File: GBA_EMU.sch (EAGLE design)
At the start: 103 parts, among them J1 USB-MINIB-5PIN, J2 AVR_SPI, SW1 LEFT, SW2 RIGHT, SW3 PWR_SWITCH, SW8 OS102011MA1Q, U1 MIC7221, U2 MCP1642B-ADJ, U4 LM4875, U5 Mic5365-2.8Y, U7 AZV321, X2 HEADPHONE

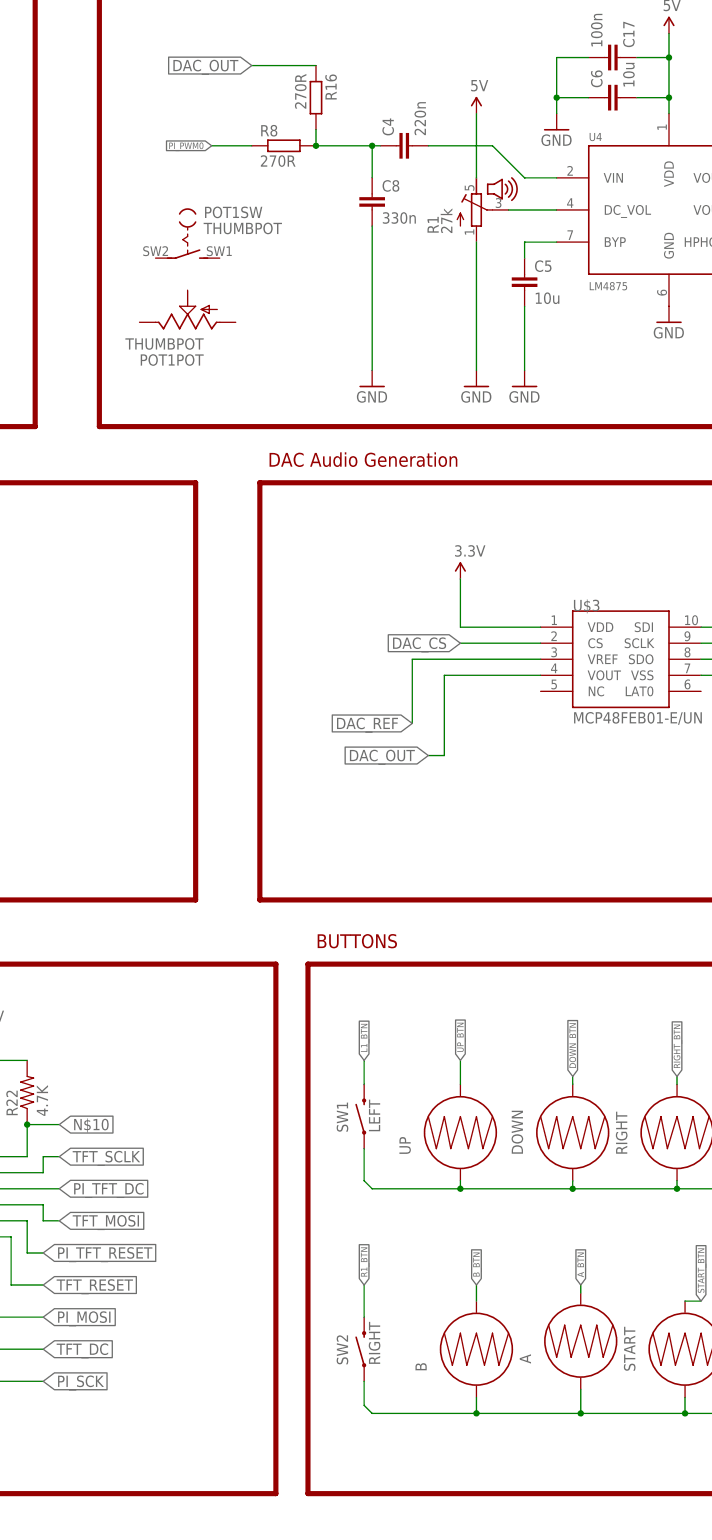
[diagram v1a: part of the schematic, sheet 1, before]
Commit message: adding more power chips
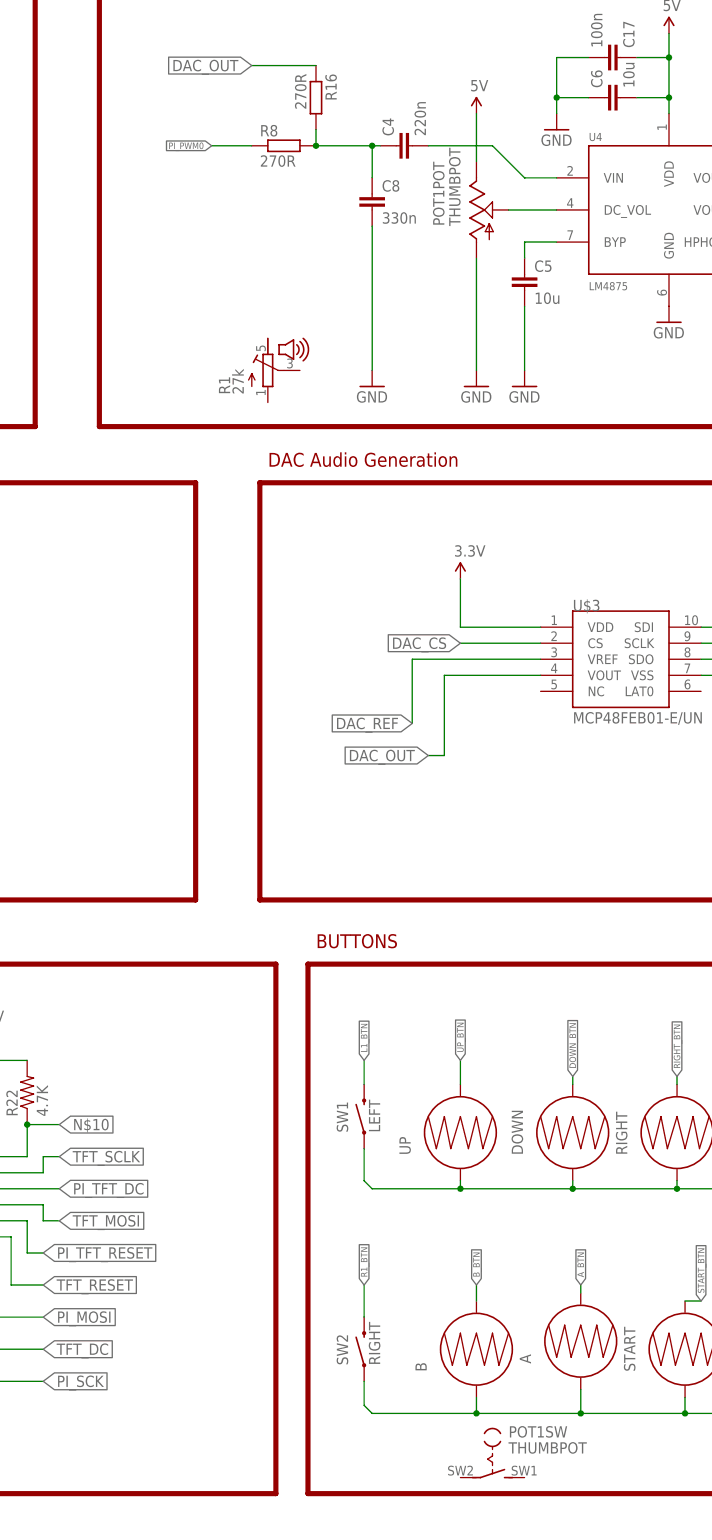
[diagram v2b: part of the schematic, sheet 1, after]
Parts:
- added J3, J4: FTDI_DEVICE, SparkFun-Connectors:FTDI_DEVICE
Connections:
- net 5V: now also POT1POT.E; no longer R1.E
- net GND: now also J3.GND, J4.GND, POT1POT.A; no longer R1.A
- net N$8: now also POT1POT.S; no longer R1.S
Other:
- note added: "FTDI Connectors"
- note removed: "MicroSD Card"
- moved on the sheet: POT1POT, POT1SW, R1
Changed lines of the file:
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@@
 <part name="D8" library="adafruit" deviceset="DIODE" device="SOD-523"/>
 <part name="SUPPLY19" library="SparkFun-Aesthetics" deviceset="3.3V" device=""/>
+<part name="J3" library="SparkFun-Connectors" deviceset="FTDI_DEVICE" device=""/>
+<part name="J4" library="SparkFun-Connectors" deviceset="FTDI_DEVICE" device=""/>
+<part name="GND40" library="SparkFun-Aesthetics" deviceset="GND" device=""/>
+<part name="GND41" library="SparkFun-Aesthetics" deviceset="GND" device=""/>
 </parts>
 <sheets>
@@
 <instance part="UP" gate="S$1" x="332.74" y="24.13" rot="R90"/>
 <instance part="START" gate="G$1" x="368.3" y="-10.16" rot="R90"/>
-<instance part="R1" gate="R$1" x="335.28" y="170.18"/>
+<instance part="R1" gate="R$1" x="302.26" y="144.78"/>
 <instance part="DOWN" gate="S$1" x="350.52" y="24.13" rot="R90"/>
 <instance part="LEFT" gate="S$1" x="383.54" y="24.13" rot="R90"/>
@@
 <instance part="R22" gate="G$1" x="264.16" y="30.48" rot="R90"/>
 <instance part="SUPPLY27" gate="G$1" x="256.54" y="38.1"/>
-<instance part="POT1" gate="SW" x="289.56" y="162.56"/>
-<instance part="POT1" gate="POT" x="289.56" y="152.4"/>
+<instance part="POT1" gate="SW" x="337.82" y="-30.48"/>
+<instance part="POT1" gate="POT" x="335.28" y="170.18" rot="R270"/>
 </instances>
 <busses>
@@
 <pinref part="GND11" gate="1" pin="GND"/>
 <wire x1="318.77" y1="167.64" x2="318.77" y2="144.78" width="0.1524" layer="91"/>
-</segment>
-<segment>
-<pinref part="R1" gate="R$1" pin="A"/>
-<pinref part="GND7" gate="1" pin="GND"/>
-<wire x1="335.28" y1="165.1" x2="335.28" y2="144.78" width="0.1524" layer="91"/>
 </segment>
 <segment>
@@
 <wire x1="464.82" y1="160.02" x2="464.82" y2="157.48" width="0.1524" layer="91"/>
 </segment>
+<segment>
+<pinref part="POT1" gate="POT" pin="A"/>
+<pinref part="GND7" gate="1" pin="GND"/>
+<wire x1="335.28" y1="162.56" x2="335.28" y2="144.78" width="0.1524" layer="91"/>
+</segment>
 </net>
 <net name="!PWREN" class="0">
@@
 </net>
 <net name="5V" class="0">
-<segment>
-<pinref part="SUPPLY2" gate="G$1" pin="5V"/>
-<pinref part="R1" gate="R$1" pin="E"/>
-<wire x1="335.28" y1="185.42" x2="335.28" y2="175.26" width="0.1524" layer="91"/>
-</segment>
 <segment>
 <pinref part="SUPPLY3" gate="G$1" pin="5V"/>
@@
 <wire x1="441.96" y1="177.8" x2="441.96" y2="195.58" width="0.1524" layer="91"/>
 </segment>
+<segment>
+<pinref part="POT1" gate="POT" pin="E"/>
+<pinref part="SUPPLY2" gate="G$1" pin="5V"/>
+<wire x1="335.28" y1="177.8" x2="335.28" y2="185.42" width="0.1524" layer="91"/>
+</segment>
 </net>
 <net name="PI_PWM0" class="0">
@@
 <wire x1="309.88" y1="182.88" x2="309.88" y2="180.34" width="0.1524" layer="91"/>
 <junction x="309.88" y="180.34"/>
-</segment>
-</net>
-<net name="N$8" class="0">
-<segment>
-<pinref part="U4" gate="U$1" pin="DC_VOL"/>
-<pinref part="R1" gate="R$1" pin="S"/>
-<wire x1="347.98" y1="170.18" x2="340.36" y2="170.18" width="0.1524" layer="91"/>
 </segment>
 </net>
@@
 <wire x1="254" y1="15.24" x2="269.24" y2="15.24" width="0.1524" layer="91"/>
 <label x="269.24" y="15.24" size="1.778" layer="95" xref="yes"/>
+</segment>
+</net>
+<net name="N$8" class="0">
+<segment>
+<pinref part="U4" gate="U$1" pin="DC_VOL"/>
+<pinref part="POT1" gate="POT" pin="S"/>
+<wire x1="347.98" y1="170.18" x2="340.36" y2="170.18" width="0.1524" layer="91"/>
 </segment>
 </net>
@@
 <wire x1="7.62" y1="7.62" x2="7.62" y2="40.64" width="0.4064" layer="94"/>
 <text x="167.64" y="170.18" size="1.778" layer="94">USB Hub</text>
-<text x="167.894" y="115.57" size="1.778" layer="94">MicroSD Card</text>
+<text x="167.894" y="115.57" size="1.778" layer="94">FTDI Connectors</text>
 <text x="8.128" y="41.656" size="1.778" layer="94">Test Points</text>
 </plain>
@@
 <instance part="D8" gate="G$1" x="127" y="91.44" rot="R180"/>
 <instance part="SUPPLY19" gate="G$1" x="30.48" y="142.24"/>
+<instance part="J3" gate="G$1" x="231.14" y="96.52"/>
+<instance part="J4" gate="G$1" x="231.14" y="66.04"/>
+<instance part="GND40" gate="1" x="223.52" y="78.74"/>
+<instance part="GND41" gate="1" x="223.52" y="48.26"/>
 </instances>
 <busses>
@@
 <pinref part="GND38" gate="1" pin="GND"/>
 </segment>
-</net>
+<segment>
+<pinref part="J3" gate="G$1" pin="GND"/>
+<wire x1="226.06" y1="88.9" x2="223.52" y2="88.9" width="0.1524" layer="91"/>
+<wire x1="223.52" y1="88.9" x2="223.52" y2="81.28" width="0.1524" layer="91"/>
+<pinref part="GND40" gate="1" pin="GND"/>
+</segment>
+<segment>
+<pinref part="J4" gate="G$1" pin="GND"/>
+<wire x1="226.06" y1="58.42" x2="223.52" y2="58.42" width="0.1524" layer="91"/>
+<wire x1="223.52" y1="58.42" x2="223.52" y2="50.8" width="0.1524" layer="91"/>
+<pinref part="GND41" gate="1" pin="GND"/>
+</segment>
+</net>

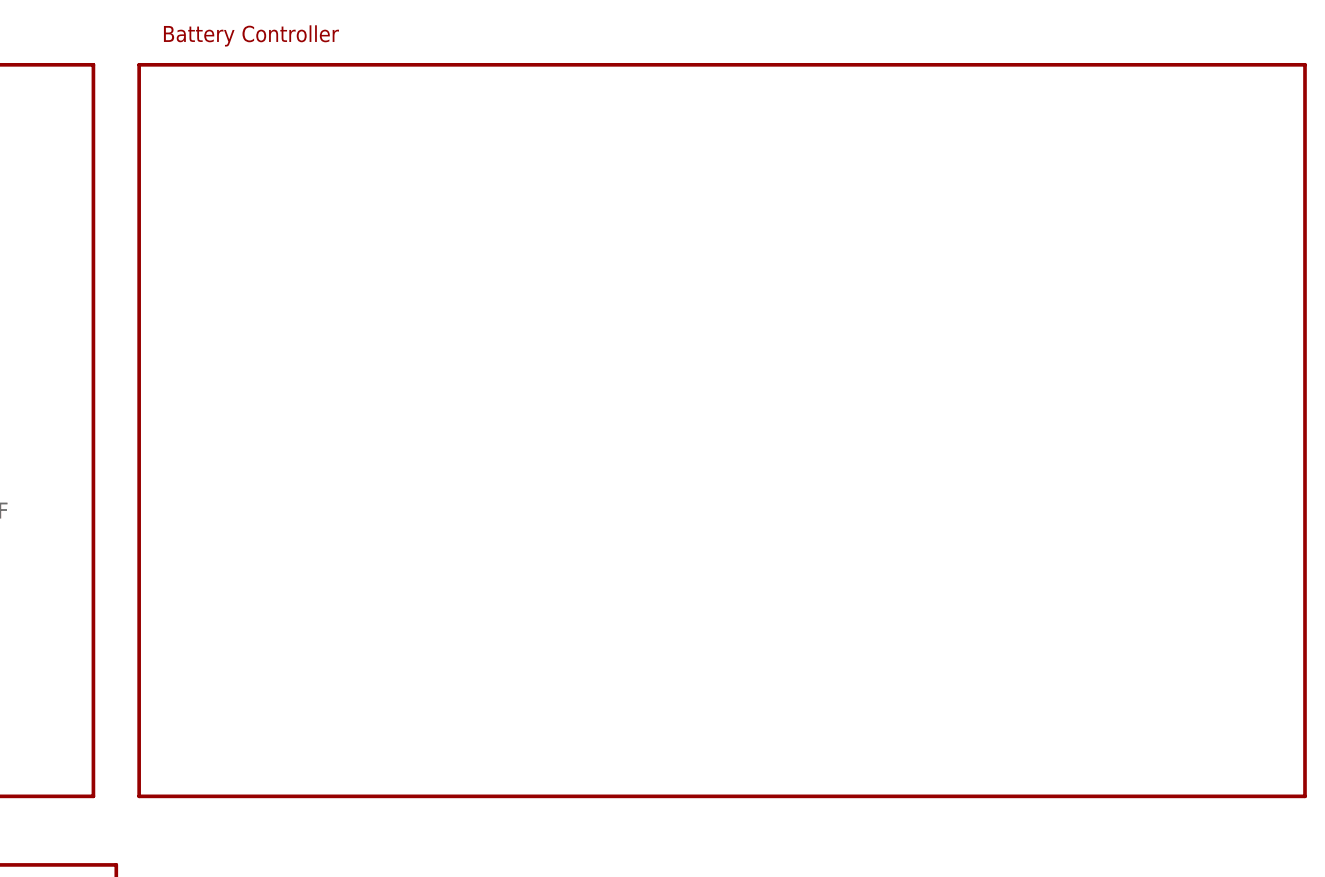
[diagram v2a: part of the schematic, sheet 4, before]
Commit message: added a few grounding caps
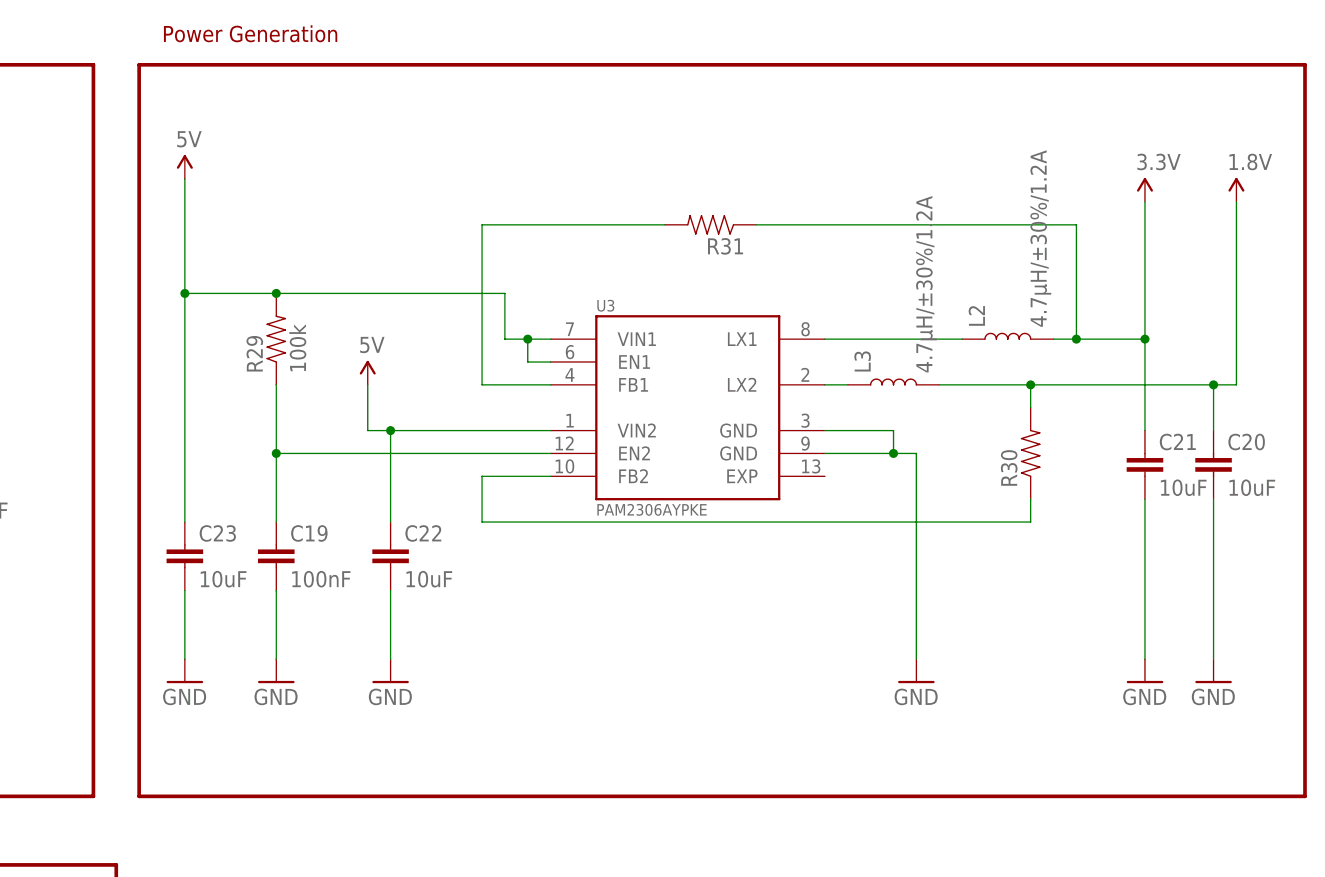
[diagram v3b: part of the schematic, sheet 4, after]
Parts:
- added C19: 100nF, SparkFun-Capacitors:10NF/10000PF-50V-10%(0603)
- added C20, C21, C22, C23: 10uF, SparkFun-Capacitors:10UF-6.3V-20%(0603)
- added L2, L3: 4.7µH/±30%/1.2A, SparkFun-Coils:INDUCTOR-CDRH-4.7UH
- added R29: 100k, SparkFun-Resistors:100KOHM-1/10W-1%(0603)
- added R30, R31: (no value), SparkFun-Resistors:RESISTOR0805-RES
- added U3: PAM2306AYPKE, custom:PAM2306AYPKE
- J3, J4: value FTDI_DEVICE -> FTDI_DEVICERA_SMT; device SparkFun-Connectors:FTDI_DEVICE -> SparkFun-Connectors:FTDI_DEVICERA_SMT
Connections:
- new net N$32: L3.1, U3.LX2
- new net N$46: C19.1, R29.1, U3.EN2
- new net N$47: L2.1, U3.LX1
- new net N$49: R31.2, U3.FB1
- new net N$50: R30.1, U3.FB2
- net 1.8V: now also C20.1, L3.2, R30.2
- net 3.3V: now also C21.1, L2.2, R31.1
- net 5V: now also C22.1, C23.1, R29.2, U3.EN1, U3.VIN1, U3.VIN2
- net GND: now also C19.2, C20.2, C21.2, C22.2, C23.2, U3.GND@1, U3.GND@2
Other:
- note added: "Power Generation"
- note removed: "Battery Controller"

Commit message: changed advanced schematic to Pi64 and added Ryan's version
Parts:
- removed C19: 100nF, SparkFun-Capacitors:10NF/10000PF-50V-10%(0603)
- removed C20, C21, C22, C23: 10uF, SparkFun-Capacitors:10UF-6.3V-20%(0603)
- removed COPRO: MEGA16u2, adafruit:ATMEGA32U2-TQFP
- removed D4, D7, D8: (no value), adafruit:DIODESOD-523
- removed D5, D6: DIODE_DFLS130L, custom:DIODE_DFLS130L
- removed FAN: (no value), SparkFun-Connectors:M02PTH
- removed FRAME2: FRAME-LEDGER, SparkFun-Aesthetics:FRAME-LEDGER
- removed J1: USB-MINIB-5PIN, SparkFun-Connectors:USB-MINIB-5PIN
- removed J2: AVR_SPI, SparkFun-Connectors:AVR_SPI_PRG_6PTH
- removed J3, J4: FTDI_DEVICERA_SMT, SparkFun-Connectors:FTDI_DEVICERA_SMT
- removed L2, L3: 4.7µH/±30%/1.2A, SparkFun-Coils:INDUCTOR-CDRH-4.7UH
- removed PCB1: RPI_COMPUTE, e14_Rpi_Compute_RevC:RPI_COMPUTE
- removed POT1: THUMBPOT, adafruit:THUMBPOT
- removed R$1: 976kR, SparkFun-Resistors:820KOHM-1/10W-1%(0603)
- removed R$8: 430kR, SparkFun-Resistors:820KOHM-1/10W-1%(0603)
- removed R16: 270R, rcl:R-EU_R0805
- removed R17, R18: 22, SparkFun-Resistors:22OHM1/10W1%(0603)
- removed R19, R24, R27, R28: 10K, SparkFun-Resistors:10KOHM-1/10W-1%(0603)0603
- removed R20: 680, SparkFun-Resistors:680OHM1/10W5%(0603)
- removed R21, R22, R25, R26: 4.7K, SparkFun-Resistors:4.7KOHM-1/10W-1%(0603)
- removed R23, R29: 100k, SparkFun-Resistors:100KOHM-1/10W-1%(0603)
- removed R30, R31: (no value), SparkFun-Resistors:RESISTOR0805-RES
- removed SW4, SW5: (no value), adafruit:SWITCH_PUSHBUTTONEVQ-PE
- removed SW6, SW7: (no value), adafruit:SWITCH_PUSHBUTTONSOFTTOUCHSMD_SJ
- removed SW8: OS102011MA1Q, adafruit:OS102011MA1Q
- removed T1: (no value), custom:TRANSISTOR_PNP_DRIVERMUN2111T1SC59-BEC
- removed TM1: (no value), adafruit:TRIMPOTTC33X
- removed TP1, TP2, TP3, TP4, TP5, TP6, TP7: PTR1TP12R, testpad:PTR1TP12R
- removed U$1: CBT3244AD, custom:CBT3244AD
- removed U$2: LOGO2INCH_SVG, custom:LOGO2INCH_SVG
- removed U$3: MCP48FEB01-E/UN, custom:MCP48FEB01-E/UN
- removed U$5: CRYSTAL-ABLS, custom:CRYSTAL-ABLS
- added L4: 4.7uH, rcl:L-EUWE-TPC
- added Q1: MOSFET-PCHANNEL, SparkFun-DiscreteSemi:MOSFET-PCHANNEL
- added U6: MIC7221, SparkFun-AnalogIC:MIC7221
- BT1: value (none) -> ~3V; device custom:GBA_BATTERY -> GBA:BATTERY
- C1: value 100nF -> 100n; device SparkFun-Capacitors:CAP0603-CAP -> rcl:C-EUC0805
- C10: value 1.0uF -> 47uF; device SparkFun-Capacitors:1.0UF-16V-10%(0603) -> rcl:CPOL-EU153CLV-0405
- C11, C12: value 22pF -> 100n; device SparkFun-Capacitors:22PF-50V-5%(0603) -> rcl:C-EUC0805
- C14: value 47uF -> 10u; device SparkFun-Capacitors:47UF-10V-10%(TANT) -> rcl:C-EUC0805
- C16: value 47uF -> 100n; device SparkFun-Capacitors:47UF-10V-10%(TANT) -> rcl:C-EUC0805
- C2: value 100nF -> 10u; device SparkFun-Capacitors:CAP0603-CAP -> rcl:C-EUC0805
- C3: value 100nF -> 100n; device SparkFun-Capacitors:10PF-50V-5%(0603) -> rcl:C-EUC0805
- C9: value 4.7u -> 47uF; device rcl:C-EUC1608 -> rcl:CPOL-EU153CLV-0405
- D1: value DUAL_LED -> DFLS130L; device custom:DUAL_LED -> diode:DFLS130L
- D2: value (none) -> DFLS130L; device adafruit:DIODESOD-523 -> diode:DFLS130L
- D3: value (none) -> DUAL_LED; device adafruit:DIODESOD-523 -> GBA:DUAL_LED
- L1: value 4.7uH -> 600; device SparkFun-Passives:INDUCTORINDUCTOR_4.7UH -> SparkFun-Passives:INDUCTOR0805
- R11: value 100K -> 47k; device rcl:R-US_R0805 -> adafruit:TRIMPOTTC33X
- R12: value 1K -> 620R; device SparkFun-Resistors:1KOHM-1/10W-1%(0603) -> rcl:R-EU_R0805
- R13: value 4.7K -> 620R; device SparkFun-Resistors:4.7KOHM-1/10W-1%(0603) -> rcl:R-EU_R0805
- R14: value 100K -> 100k; device rcl:R-US_R0805 -> rcl:R-EU_R0805
- R15: value 100K -> 270R; device rcl:R-US_R0805 -> rcl:R-EU_R0805
- R2: value 4.7K -> 27R; device SparkFun-Resistors:4.7KOHM-1/10W-1%(0603) -> rcl:R-EU_R0805
- R3: value 100k -> 27R; device SparkFun-Resistors:100KOHM-1/10W-1%(0603) -> rcl:R-EU_R0805
- R4: value 270 -> 1k; device SparkFun-Resistors:287OHM-1/10W-1%(0603) -> rcl:R-EU_R0805
- R5: value 680 -> 100k; device SparkFun-Resistors:680OHM1/10W5%(0603) -> rcl:R-EU_R0805
- R7: value 0R -> 976k; device rcl:R-EU_R2012 -> rcl:R-EU_R0805
- R9: value 100K -> 430k; device rcl:R-US_R0805 -> rcl:R-EU_R0805
- U1: value MIC7221 -> RPI-ZERO; device custom:SPARKFUN-ANALOGIC_MIC7221 -> RPI-Zero:RPI-ZERO
- U2: value MCP1642B-ADJ -> FT230X; device custom:MICROCHIP_MCP1642B-ADJ -> ftdichip:FT230X
- U3: value PAM2306AYPKE -> MCP1642B-ADJ; device custom:PAM2306AYPKE -> microchip:MCP1642B-ADJ
- U5: value Mic5365-2.8Y -> V_REG_LDOSMD2
- X1: value (none) -> LINK_SOCKET; device Adafruit_PowerBoost:MICROBUILDER_USB_TYPEAPTHFML -> GBA:LINK_SOCKET
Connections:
- removed net 1.8V: C20.1, L3.2, PCB1.183/1V8, PCB1.184/1V8, PCB1.185/1V8, PCB1.186/1V8, R30.2, TP5.TP
- removed net BATT_LOW: D1.1, D1.3, D8.A, R3.2, U1.OUT1
- removed net COPRO_D+: R18.1
- removed net COPRO_D-: R17.1
- removed net COPRO_DC: COPRO.PB6(PCINT6), U$1.1A4
- removed net COPRO_MISO: COPRO.PB3(PDO/MISO/PCINT3), J2.1, U$3.SDO
- removed net COPRO_MOSI: COPRO.PB2(PDI/MOSI/PCINT2), J2.4, U$1.1A2, U$3.SDI
- removed net COPRO_RESET: COPRO./RESET(PC1), J2.5, R19.1
- removed net COPRO_RX: COPRO.PD2(INT2/AIN1/RXD1)
- removed net COPRO_SCK: COPRO.PB1(SCK/PCINT1), J2.3, U$1.1A1, U$3.SCLK
- removed net COPRO_TFT_RESET: COPRO.PB0(SS/PCINT0), U$1.1A3
- removed net COPRO_TX: COPRO.PD3(INT3/TXD1)
- removed net DAC_CS: COPRO.PB5(PCINT5), U$3.CS
- removed net DAC_OUT: R16.1, U$3.VOUT
- removed net DAC_REF: U$3.VREF
- removed net DOWN_BTN: DOWN.2, PCB1.59/GPIO17
- removed net EMMC_DISABLE: PCB1.2/EMMC_DISABLE_N
- removed net FAN_EN: R12.2
- removed net HDMI_CEC: PCB1.171/HDMI_CEC
- removed net HDMI_CLK_N: PCB1.111/HDMI_CK_N*
- removed net HDMI_CLK_P: PCB1.113/HDMI_CK_P*
- removed net HDMI_D0_N: PCB1.117/HDMI_D0_N*
- removed net HDMI_D0_P: PCB1.119/HDMI_D0_P*
- removed net HDMI_D1_N: PCB1.123/HDMI_D1_N*
- removed net HDMI_D1_P: PCB1.125/HDMI_D1_P*
- removed net HDMI_D2_N: PCB1.129/HDMI_D2_N*
- removed net HDMI_D2_P: PCB1.131/HDMI_D2_P*
- removed net HDMI_SCLK: PCB1.175/HDMI_SCL
- removed net HDMI_SDA: PCB1.173/HDMI_SDA
- removed net L1_BTN: PCB1.21/GPIO6, SW1.2
- removed net L2_BTN: PCB1.57/GPIO16, R2.1, SW4.P$1
- removed net LEFT_BTN: LEFT.2, PCB1.89/GPIO27
- removed net N$17: PCB1.28/GPIO28, R9.2
- removed net N$26: R14.2
- removed net N$27: R15.2
- removed net N$28: C11.1, COPRO.XTAL1, U$5.P$2
- removed net N$29: C12.1, COPRO.XTAL2/PC0, U$5.P$1
- removed net N$30: PCB1.179/VDD_CORE
- removed net N$31: D3.A, D4.C
- removed net N$32: L3.1, U3.LX2
- removed net N$33: D3.C, D7.C, R27.2, R28.2
- removed net N$34: L1.2, U2.SW
- removed net N$35: PCB1.177/RUN
- removed net N$36: PCB1.197/VBAT, PCB1.199/VBAT
- removed net N$37: PCB1.198/VBAT, PCB1.200/VBAT
- removed net N$38: COPRO.PC7(ICP1/INT4/CLKO), R27.1
- removed net N$39: FAN.1, T1.C
- removed net N$40: R12.1, T1.B
- removed net N$41: PCB1.23/GPIO7
- removed net N$42: PCB1.27/GPIO8
- removed net N$43: PCB1.29/GPIO9
- removed net N$44: COPRO.PD0(INT0/OC0B), R24.1
- removed net N$45: C14.+, D5.C, D6.C, L1.1, SW8G$1.P, U2.VIN
- removed net N$46: C19.1, R29.1, U3.EN2
- removed net N$47: L2.1, U3.LX1
- removed net N$49: R31.2, U3.FB1
- removed net N$50: R30.1, U3.FB2
- removed net PI_MOSI: PCB1.33/GPIO10, U$1.2A2
- removed net PI_PWM0: PCB1.63/GPIO18, R8.1
- removed net PI_SCK: PCB1.35/GPIO11, U$1.2A1
- removed net PI_SHUTDOWN: PCB1.69/GPIO20
- removed net PI_TFT_DC: PCB1.11/GPIO3, U$1.2A4
- removed net PI_TFT_RESET: PCB1.9/GPIO2, U$1.2A3
- removed net PWR_DOWN: D2.A, D4.A, SW8G$1.S
- removed net PWR_UP: D2.C, R23.2, R24.2, U2.EN
- removed net R1_BTN: PCB1.71/GPIO21, SW2.2
- removed net R2_BTN: PCB1.45/GPIO12, R13.1, SW5.P$1
- removed net RIGHT_BTN: PCB1.75/GPIO22, RIGHT.2
- removed net SELECT_BTN: PCB1.81/GPIO24, SEL.2
- removed net START_BTN: PCB1.77/GPIO23, START.2
- removed net TFT_SCLK: TFT1.SCL, U$1.1B1, U$1.2B1
- removed net UP_BTN: PCB1.17/GPIO5, UP.2
- removed net USB_GND: J1.GND
- removed net V_BATT: BT1.+, D6.A, R4.2
- removed net V_USB: D5.A, J1.VBUS
- removed net X_BTN: PCB1.83/GPIO25, R26.1, SW6.P$1
- removed net Y_BTN: PCB1.47/GPIO13, R25.1, SW7.P$1
- new net !PWREN: C3.2, Q1.G, R4.1, R5.2
- new net 0.8128: C9.+, L4.1, SW3.P, U3.EN, U3.VIN
- new net 3.3V_FTDI: C1.1, U2.!RESET, U2.3V3OUT, U2.VCCIO
- new net 5V_FTDI: C14.1, C2.1, L1.1, Q1.S, R5.1, U2.VCC
- new net DOWN: DOWN.2, U1.GPIO17/GEN0
- new net LEFT: LEFT.2, U1.GPIO27/GEN2
- new net LEFT_BUMP: SW1.2, U1.GPIO6
- new net PWM0: R8.1, U1.GPIO18
- new net RIGHT: RIGHT.2, U1.GPIO22/GEN3
- new net RIGHT_BUMP: SW2.2, U1.GPIO21
- new net SELECT: SEL.2, U1.GEN5/GPIO24
- new net START: START.2, U1.GEN4/GPIO23
- new net TFT_SCK: TFT1.SCL, U1.GPIO11/SCLK
- new net UP: U1.GPIO5, UP.2
- new net USB_5V: C3.1, D1.A, Q1.D
- new net V_BAT: BT1.+, D2.A, R15.2
- net 2.8V: no longer TP3.TP
- net 3.3V: now also U1.3V3@1; no longer C21.1, COPRO.AVCC, COPRO.UVCC, COPRO.VCC, L2.2, PCB1.191/3V3, PCB1.192/3V3, PCB1.193/3V3, PCB1.194/3V3, PCB1.39/GPIO0-27_VREF, PCB1.40/GPIO0-27_VREF, R13.2, R2.2, R21.2, R22.2, R25.2, R26.2, R31.1, R7.2, TP2.TP, U$1.VCC, U$3.VDD
- net 5V: now also C10.+, C16.1, R1.E, R11.E, R13.2, R7.2, U1.5V0@1, U1.5V0@2, U3.VOUT, U6.+V; no longer C16.+, C22.1, C23.1, C3.1, FAN.2, J2.2, POT1POT.E, R$1.2, R19.2, R29.2, R5.2, TM1.E, TP1.TP, U1.+V, U2.VOUT, U3.EN1, U3.VIN1, U3.VIN2, X1.VBUS
- net A_BTN: now also U1.GPIO19; no longer PCB1.65/GPIO19
- net B_BTN: now also U1.GPIO26; no longer PCB1.87/GPIO26
- net GND: now also C10.-, C14.2, C16.2, C9.-, R1.A, R11.A, R12.2, U1.GND@2, U1.GND@3, U1.GND@4, U1.GND@5, U1.GND@6, U1.GND@7, U1.GND@8, U2.GND@1, U2.GND@2, U3.GND, U6.GND, X1.1; no longer C10.2, C14.-, C16.-, C19.2, C20.2, C21.2, C22.2, C23.2, C3.2, C9.2, COPRO.GND, COPRO.UGND, J2.6, J3.GND, J4.GND, PCB1.1/GND, PCB1.103/GND, PCB1.104/GND, PCB1.109/GND, PCB1.110/GND, PCB1.115/GND, PCB1.116/GND, PCB1.121/GND, PCB1.122/GND, PCB1.127/GND, PCB1.13/GND, PCB1.133/GND, PCB1.134/GND, PCB1.139/GND, PCB1.14/NC, PCB1.140/GND, PCB1.145/GND, PCB1.146/GND, PCB1.151/GND, PCB1.152/GND, PCB1.157/GND, PCB1.163/GND, PCB1.164/GND, PCB1.169/GND, PCB1.170/GND, PCB1.181/GND, PCB1.182/GND, PCB1.187/GND, PCB1.188/GND, PCB1.19/GND, PCB1.195/GND, PCB1.196/GND, PCB1.20/NC, PCB1.25/GND, PCB1.26/GND, PCB1.31/GND, PCB1.32/GND, PCB1.37/GND, PCB1.38/GND, PCB1.43/GND, PCB1.44/GND, PCB1.49/GND, PCB1.50/GND, PCB1.55/GND, PCB1.56/GND, PCB1.61/GND, PCB1.62/GND, PCB1.67/GND, PCB1.68/GND, PCB1.7/GND, PCB1.73/GND, PCB1.74/GND, PCB1.79/GND, PCB1.8/NC, PCB1.80/GND, PCB1.85/GND, PCB1.86/GND, PCB1.91/GND, PCB1.92/GND, PCB1.97/GND, PCB1.98/GND, POT1POT.A, R$8.1, R11.1, R14.1, R15.1, R20.1, R23.1, SW4.P$2, SW5.P$2, SW6.P$2, SW7.P$2, T1.E, TM1.A, TP4.TP, U$1.GND, U$3.VSS, U1.GND, U2.GND, U3.GND@1, U3.GND@2
- net N$1: now also C11.1, R11.S, R14.2, U6.+IN1; no longer C9.1, PCB1.4/NC, PCB1.6/NC, R7.1
- net N$10: now also R4.2, U2.CBUS3; no longer R22.1, U$1.2!OE
- net N$12: now also L4.2, U3.SW; no longer COPRO.PC2(AIN2/PCIN11), R28.1
- net N$18: now also D1.C, D2.C, SW3.O; no longer R21.1, U$1.!1OE
- net N$19: now also D3.1, D3.3, R14.1, U6.OUT1; no longer COPRO.D-, R17.2
- net N$2: no longer R16.2
- net N$20: now also R7.1, R9.2, U3.VFB; no longer PCB1.30/GPIO29, R11.2
- net N$22: now also D3.4, R13.1; no longer COPRO.D+, R18.2
- net N$23: now also D3.2, R12.1; no longer R$1.1, R$8.2, U2.VFB
- net N$25: now also C12.1, R15.1, U6.-IN1; no longer C10.1, COPRO.UCAP
- net N$3: now also L1.2, X1.3, X1.5, X1.6; no longer D7.A, D8.C
- net N$4: now also R2.2, X1.4; no longer C2.1, R3.1, TM1.S, U1.+IN1
- net N$5: now also R3.2, X1.2; no longer C1.1, R4.1, U1.-IN1
- net N$6: now also R2.1, U2.USBDM; no longer D1.4, R5.1
- net N$7: now also R3.1, U2.USBDP; no longer D1.2, R20.2
- net N$8: now also R1.S; no longer POT1POT.S
- net RXD: now also U1.TXD0/GPIO14, U2.RXD; no longer PCB1.53/GPIO15
- net TFT_CS: now also U1.!CE0!/GPIO8; no longer COPRO.PD4(INT5/AIN3)
- net TFT_DC: now also U1.GPIO3/SCL1; no longer U$1.1B4, U$1.2B4
- net TFT_LED: now also U1.GPIO4/GCKL; no longer PCB1.15/GPIO4
- net TFT_MOSI: now also U1.GPIO10/MOSI; no longer U$1.1B2, U$1.2B2
- net TFT_RESET: now also U1.GPIO2/SDA1; no longer U$1.1B3, U$1.2B3
- net TXD: now also U1.RXD0/GPIO15, U2.TXD; no longer PCB1.51/GPIO14
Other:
- note added: "ADJUST TRIMMER TO OUTPUT 2V. THIS SETS THE BATTERY VOLTAGE TO TURN THE LED RED"
- note added: "BT1 POWER PROVIDED FROM 2xAA ALKALINE BATTERIES"
- note added: "BY RYAN WENDLAND"
- note added: "GBA_EMU"
- note added: "HYSTERESIS"
- note added: "MAY 2016"
- note added: "POWER LED INDICATION"
- note added: "POWER OR'ING"
- note added: "Place C10 as close as possible to Vout on U3."
- note added: "USB SERIAL INTERFACE"
- note removed: "BY MATTHEW CARLSON"
- note removed: "Boost Converter"
- note removed: "Bus Switch"
- note removed: "C16 as close to VOUT as possible"
- note removed: "Coprocessor"
- note removed: "DAC Audio Generation"
- note removed: "FAN"
- note removed: "FTDI Connectors"
- note removed: "GBA_EMU NOV 2016"
- note removed: "Hysteresis"
- note removed: "POWER LED INDICATOR"
- note removed: "Power Generation"
- note removed: "Power Or'ing"
- note removed: "Set the trim pot so the LED turns red at 2v"
- note removed: "TFT Power Generation"
- note removed: "Test Points"
- note removed: "USB Hub"
- note removed: "VIA RYAN WENDLAND"
